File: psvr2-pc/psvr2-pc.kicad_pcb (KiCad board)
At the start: 4 copper layers, 101.3 x 63.5 mm, 109 parts, among them IC1 SN65MLVD200D, IC2 SN65MLVD200D, J1 USB_C_Receptacle, J2 USB3_B_Micro, J3 DP_47272, J4 Barrel_Jack_Switch, J5 Conn_01x02_Pin, Q1 Si2301CDS, Q2 PN2222A, Q3 Si2301CDS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

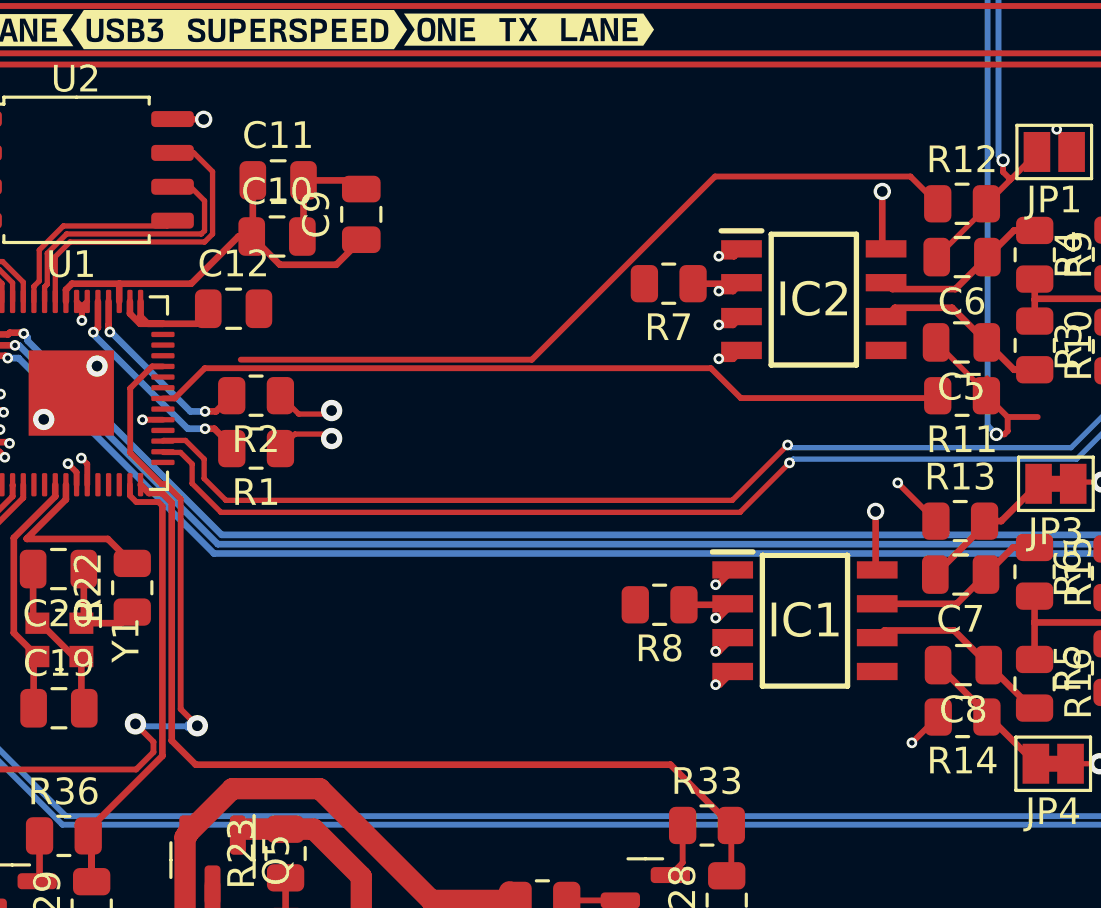
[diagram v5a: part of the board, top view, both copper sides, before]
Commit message: Route the DP-AUX pull-up/pull-down GPIOs, had to switch them around for the traces to line up without overlapping. Make it do a nice pattern/shape, surrounding each island. Why not.
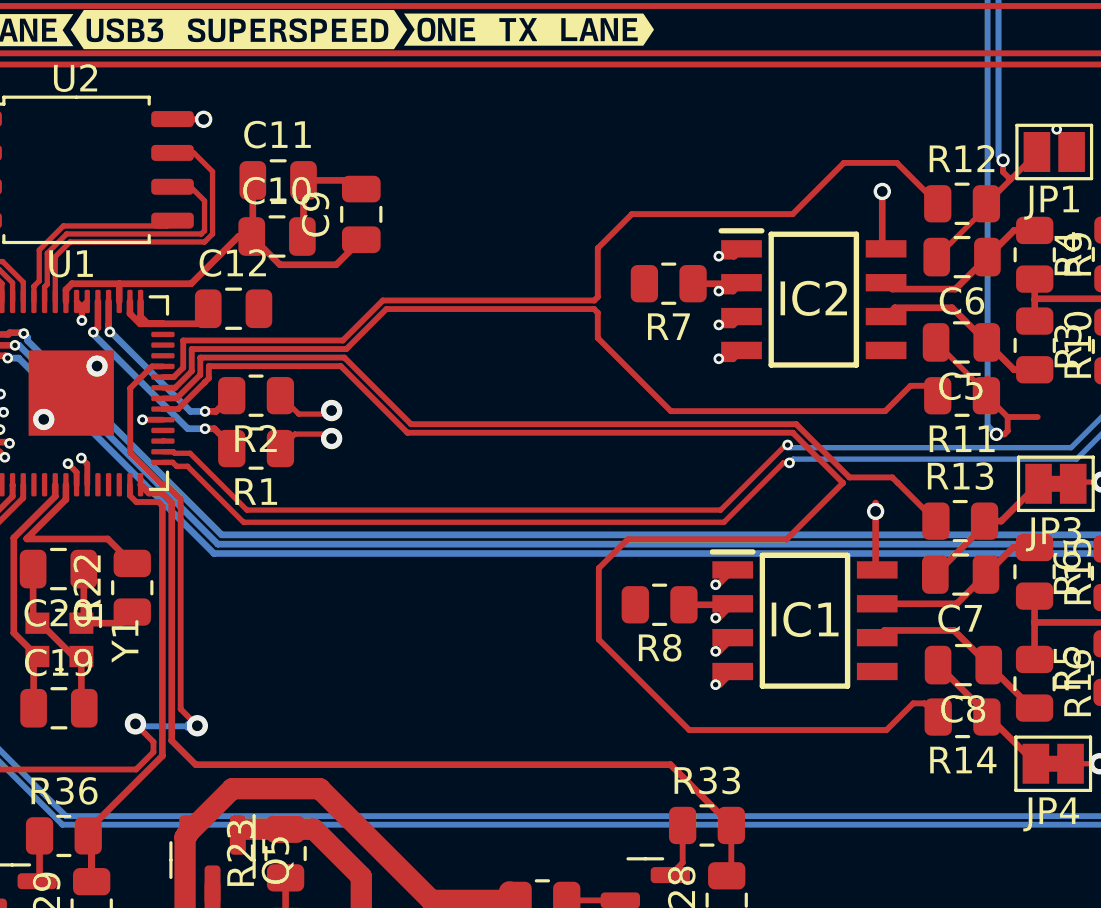
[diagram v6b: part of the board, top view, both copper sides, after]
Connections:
- U1 pad 29: unconnected-(U1-GPIO18-Pad29) -> /HMD_USB2_P
- U1 pad 30: /HMD_USB2_P -> /HMD_USB2_N
- U1 pad 31: /HMD_USB2_N -> unconnected-(U1-GPIO20-Pad31)
- U1 pad 34: /PC_AUX_TERMINATION_P -> /HMD_AUX_TERMINATION_N
- U1 pad 35: /PC_AUX_TERMINATION_N -> /HMD_AUX_TERMINATION_P
- U1 pad 36: /HMD_AUX_TERMINATION_P -> /PC_AUX_TERMINATION_N
- U1 pad 37: /HMD_AUX_TERMINATION_N -> /PC_AUX_TERMINATION_P
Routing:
- net +3.3V: track 62.6 -> 78.6 mm
- net /HMD_AUX_TERMINATION_N: track 62.2 -> 56.2 mm, vias 1 -> 0
- net /PC_AUX_TERMINATION_P: track 29.4 -> 34.7 mm
- net /PC_AUX_TERMINATION_N: track 30.0 -> 33.5 mm
- net /HMD_AUX_TERMINATION_P: track 34.2 -> 32.5 mm, vias 1 -> 0

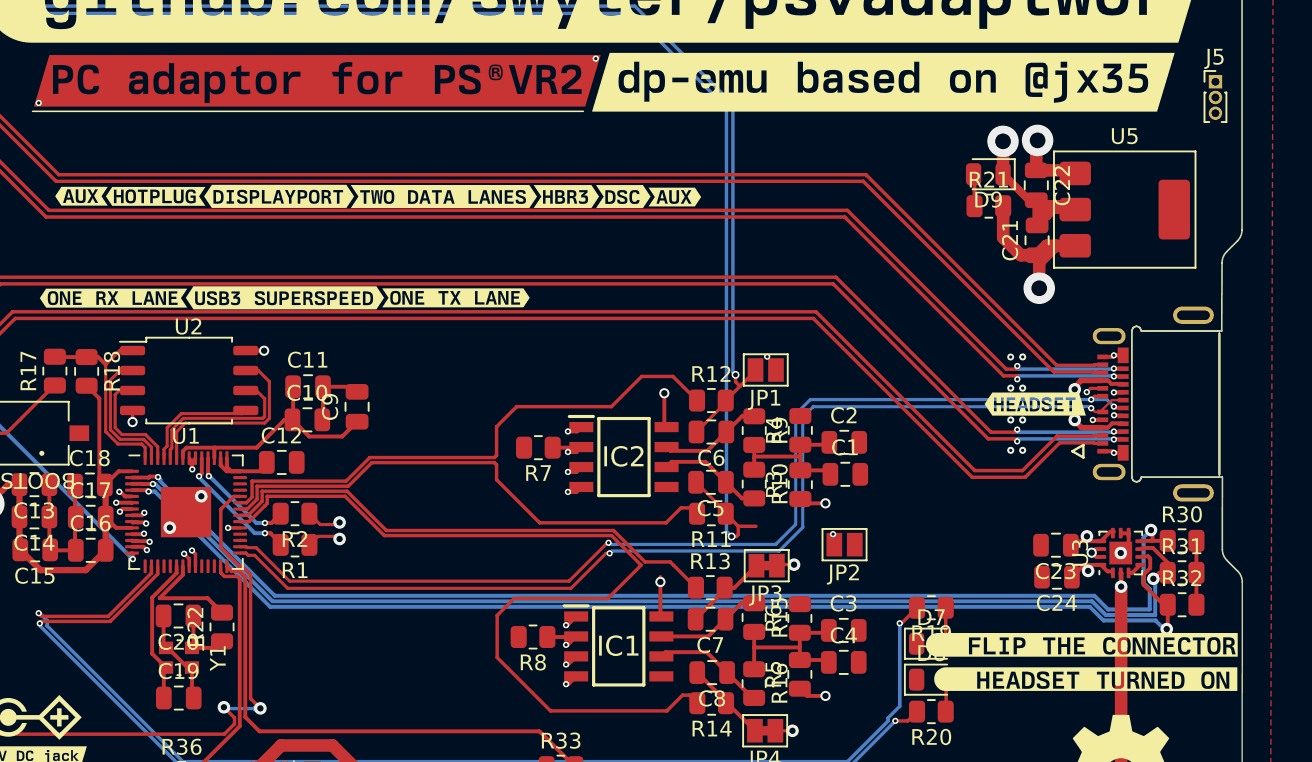
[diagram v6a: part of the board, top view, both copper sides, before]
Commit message: Almost there, only a couple nets/traces left.
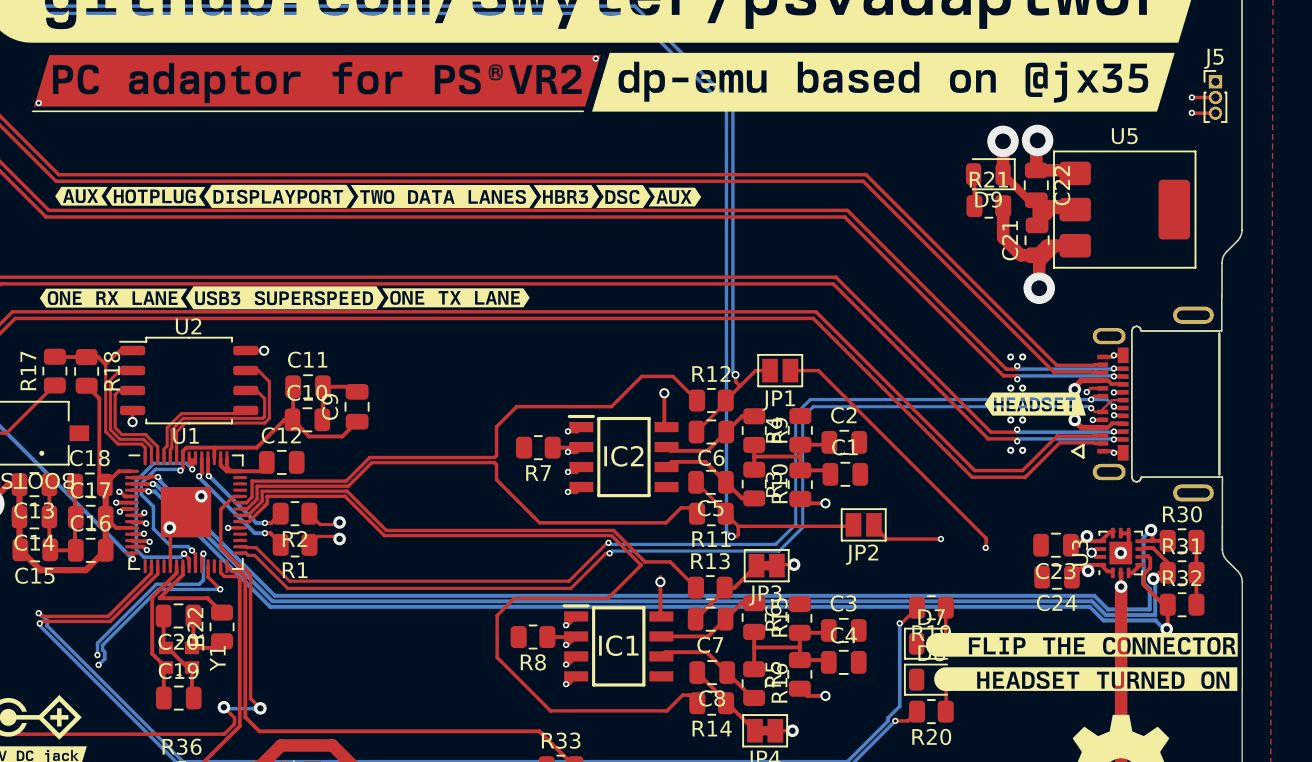
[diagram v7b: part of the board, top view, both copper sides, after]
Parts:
- moved JP2 1.75 mm to (89.9, 51.4)
- moved JP1 0.92 mm to (84.6, 41.6)
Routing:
- net /HMD_AUX_P: track 48.2 -> 66.9 mm
- net /SWD: track 0.00 -> 13.7 mm, vias 0 -> 3
- net /SWCLK: track 0.00 -> 13.2 mm, vias 0 -> 3
- net +3.3V: track 78.6 -> 90.5 mm
- net +1V1: track 17.1 -> 27.0 mm, vias 1 -> 2
- net /HMD_AUX_N: track 38.0 -> 45.2 mm, vias 2 -> 3
- net /PC_AUX_N: track 90.6 -> 96.9 mm, vias 3 -> 2
- net GND: track 103.2 -> 105.7 mm
- net /PC_AUX_P: track 83.2 -> 84.1 mm

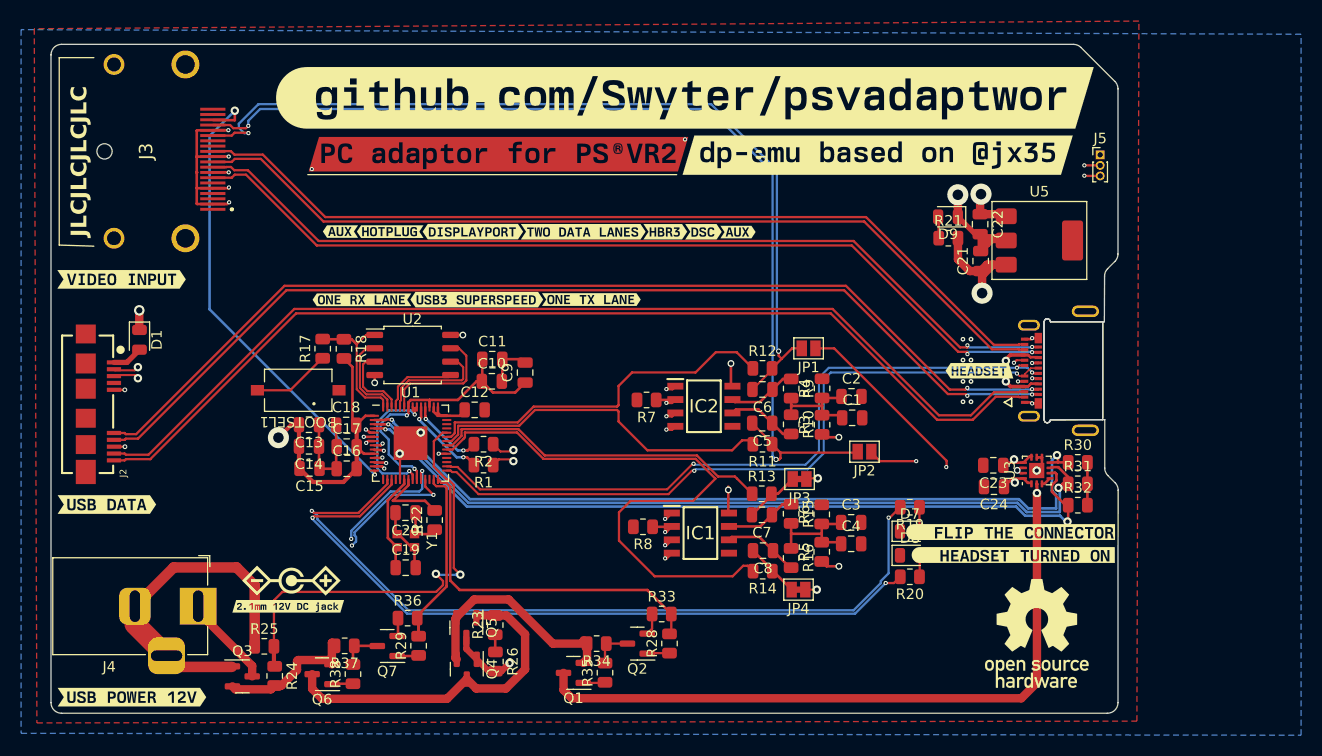
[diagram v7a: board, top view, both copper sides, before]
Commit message: Try to fix the third layer (power plane) to actually have a ground fill under/over the high-speed differential lines. route the SWD/SWCLK lines.
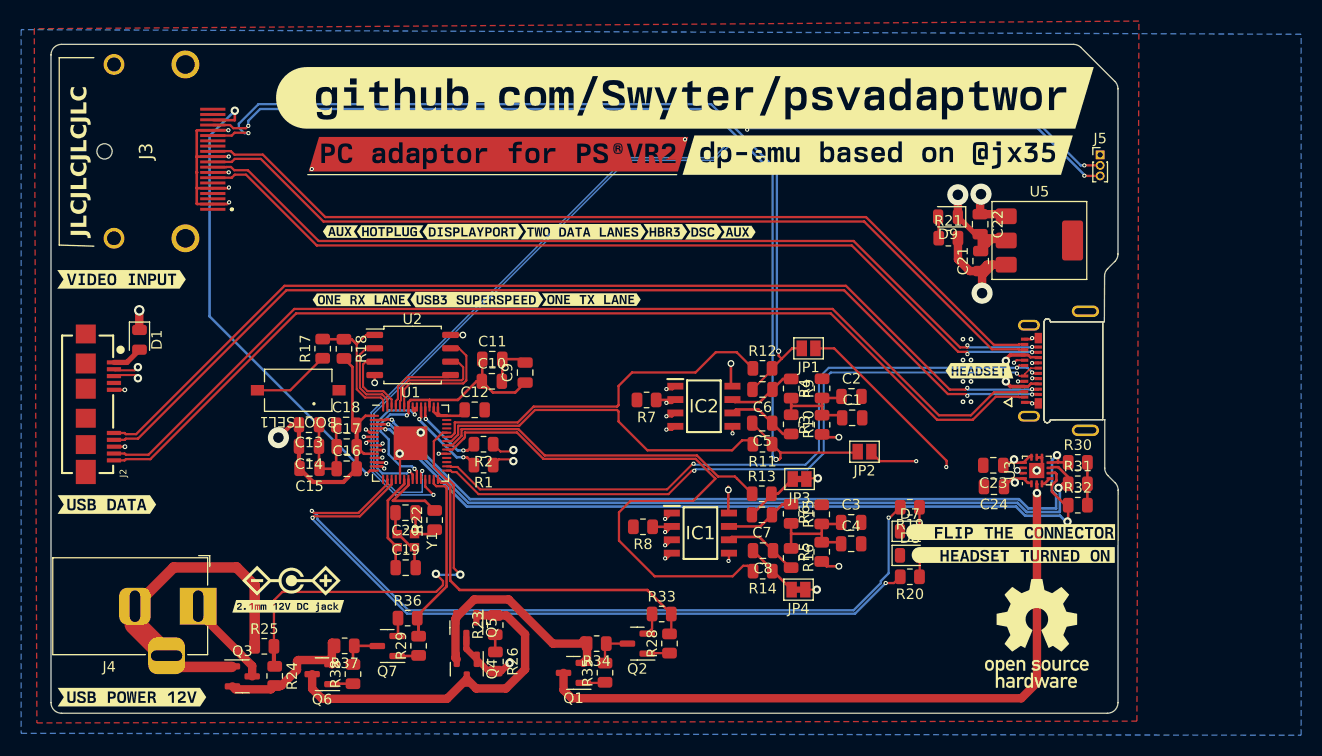
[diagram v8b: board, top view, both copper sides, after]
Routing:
- net /SWD: track 13.7 -> 96.6 mm, vias 3 -> 4
- net /SWCLK: track 13.2 -> 95.8 mm, vias 3 -> 4
- net GND: track 105.7 -> 107.1 mm, vias 24 -> 26
